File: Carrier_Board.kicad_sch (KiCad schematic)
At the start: 0 parts

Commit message: Created heirachical sheets
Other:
- added sheet Fan (Fan.kicad_sch)
- added sheet GPIO (GPIO.kicad_sch)
- added sheet Gigabit Ethernet (ethernet.kicad_sch)
- added sheet HDMI (hdmi.kicad_sch)
- added sheet LattePanda Module (LattePanda_Module.kicad_sch)
- added sheet M.2 M Key (m2_em.kicad_sch)
- added sheet PCIe x4 (pciex4.kicad_sch)
- added sheet Power Supply (PSU.kicad_sch)
- added sheet USB 2.0 & 3.0 (usb_2_3.kicad_sch)

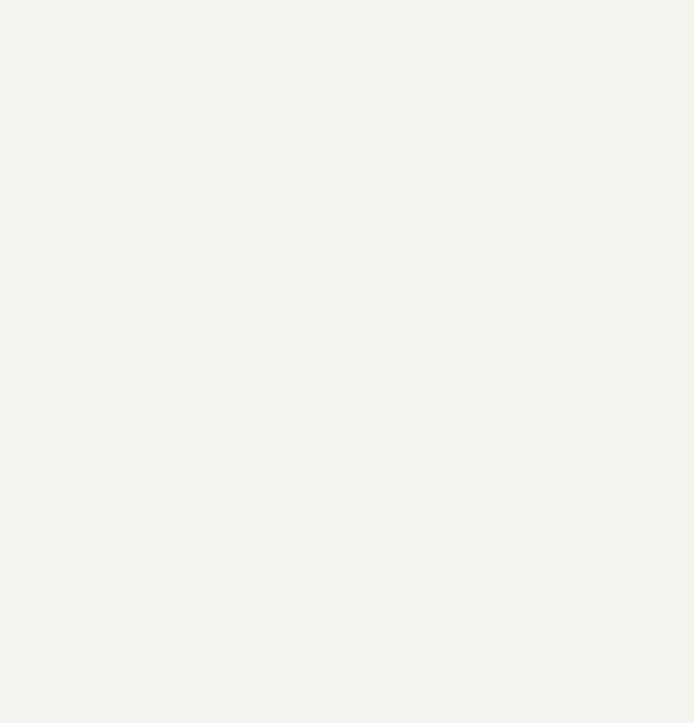
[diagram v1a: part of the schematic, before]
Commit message: Added mounting holes and Fiducials
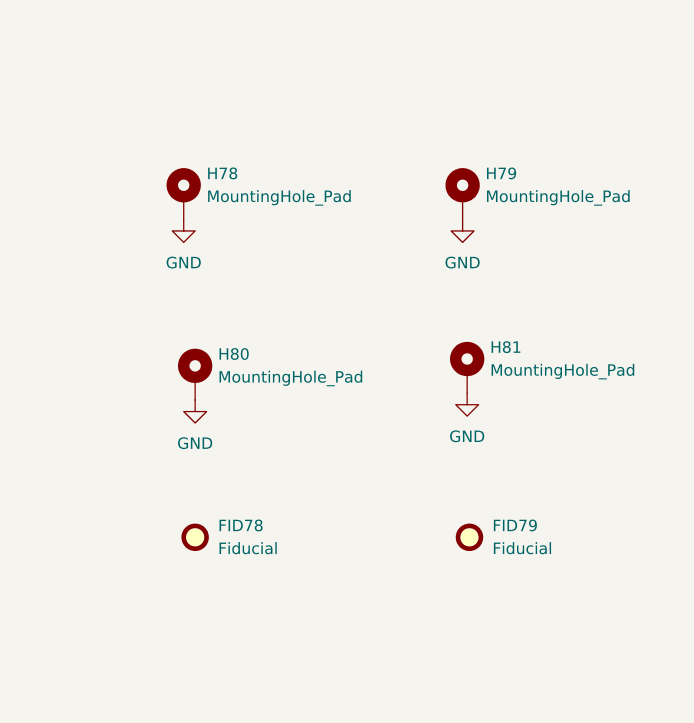
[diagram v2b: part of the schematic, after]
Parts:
- added FID78, FID79: Fiducial, symbol Mechanical:Fiducial
- added H78, H79, H80, H81: MountingHole_Pad, symbol Mechanical:MountingHole_Pad
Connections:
- new net GND: H78.1, H79.1, H80.1, H81.1

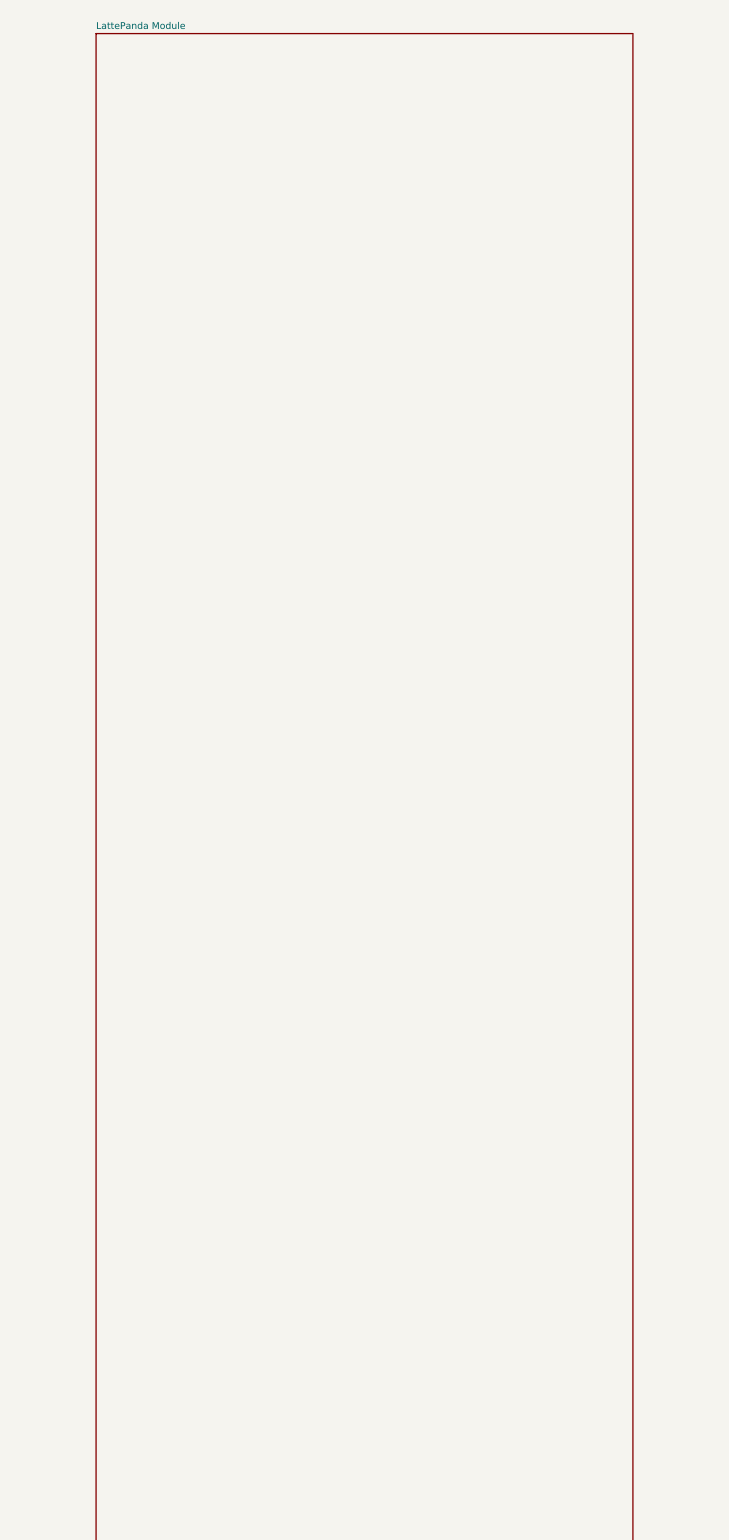
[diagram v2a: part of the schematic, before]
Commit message: Added hierachical labels to the main scheematic
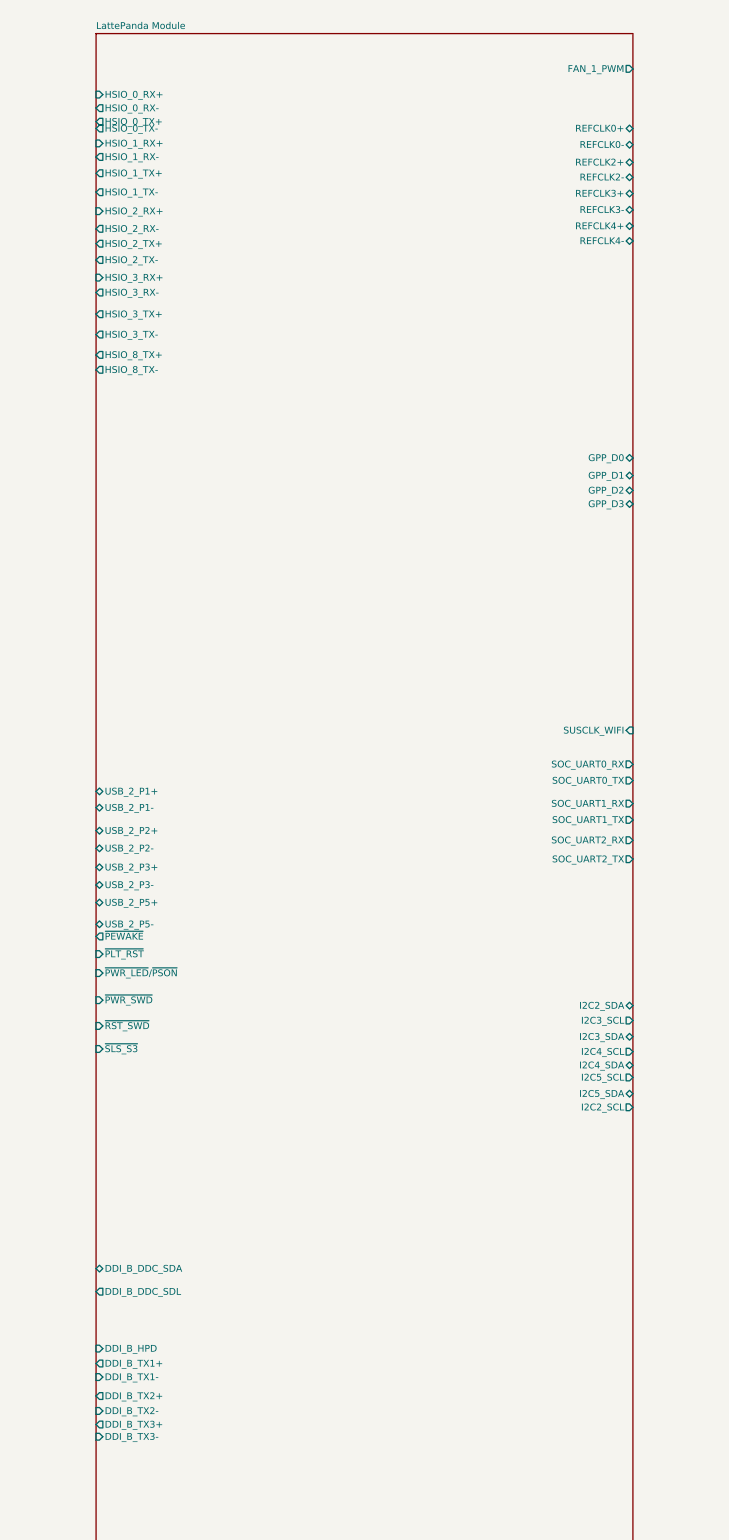
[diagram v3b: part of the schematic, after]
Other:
- sheet LattePanda Module ports: added DDI_B_DDC_SDA, DDI_B_DDC_SDL, DDI_B_HPD, DDI_B_TX1+, DDI_B_TX1-, DDI_B_TX2+, DDI_B_TX2-, DDI_B_TX3+, DDI_B_TX3-, FAN_1_PWM, GPP_D0, GPP_D1, GPP_D2, GPP_D3, HSIO_0_RX+, HSIO_0_RX-, HSIO_0_TX+, HSIO_0_TX-, HSIO_1_RX+, HSIO_1_RX-, HSIO_1_TX+, HSIO_1_TX-, HSIO_2_RX+, HSIO_2_RX-, HSIO_2_TX+, HSIO_2_TX-, HSIO_3_RX+, HSIO_3_RX-, HSIO_3_TX+, HSIO_3_TX-, HSIO_8_TX+, HSIO_8_TX-, I2C2_SCL, I2C2_SDA, I2C3_SCL, I2C3_SDA, I2C4_SCL, I2C4_SDA, I2C5_SCL, I2C5_SDA, REFCLK0+, REFCLK0-, REFCLK2+, REFCLK2-, REFCLK3+, REFCLK3-, REFCLK4+, REFCLK4-, SOC_UART0_RX, SOC_UART0_TX, SOC_UART1_RX, SOC_UART1_TX, SOC_UART2_RX, SOC_UART2_TX, SUSCLK_WIFI, USB_2_P1+, USB_2_P1-, USB_2_P2+, USB_2_P2-, USB_2_P3+, USB_2_P3-, USB_2_P5+, USB_2_P5-, ~{PEWAKE}, ~{PLT_RST}, ~{PWR_LED}/~{PSON}, ~{PWR_SWD}, ~{RST_SWD}, ~{SLS_S3}; removed none
